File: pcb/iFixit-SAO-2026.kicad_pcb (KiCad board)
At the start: 2 copper layers, 82.6 x 83.8 mm, 29 parts, among them SW1 SW_Push, U1 ATtiny1604-SS

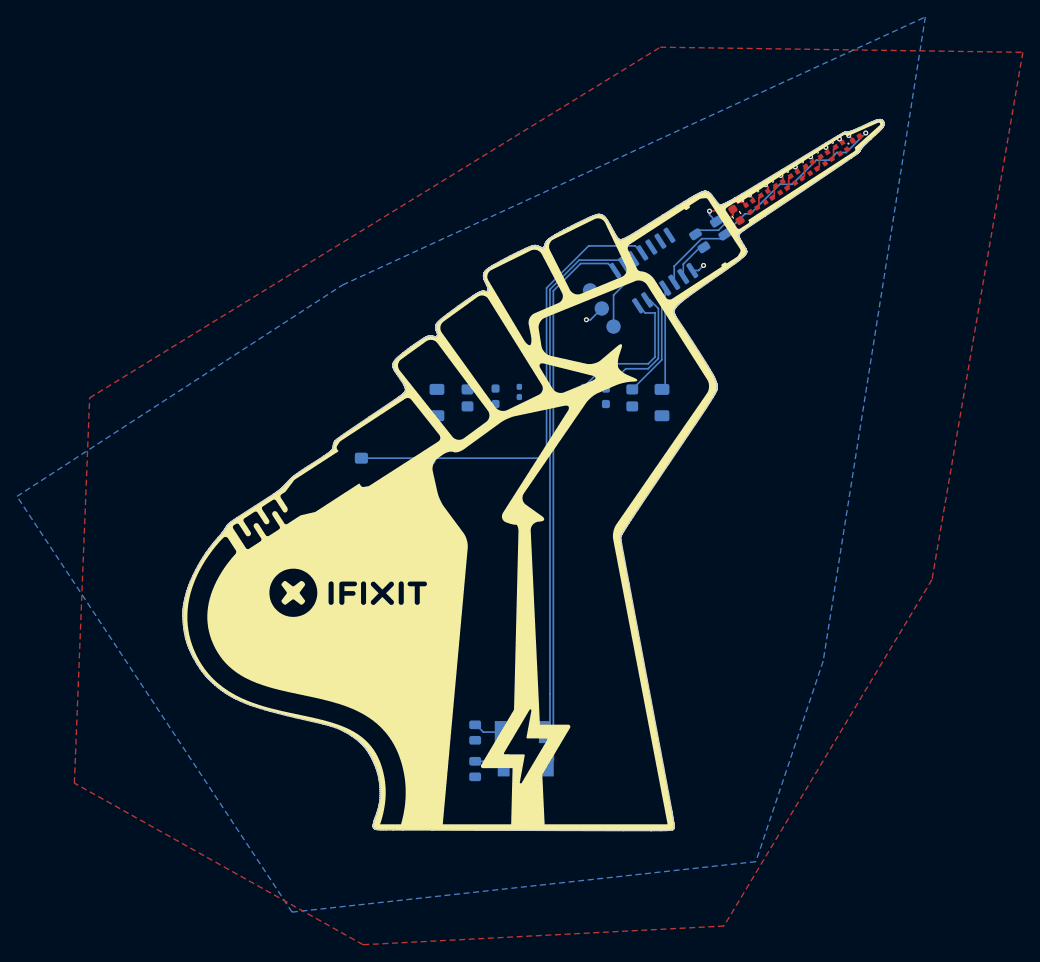
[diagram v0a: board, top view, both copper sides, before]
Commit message: Version 0.1 - FINAL: art, code, and PCB. 1000 made for DEFCON34
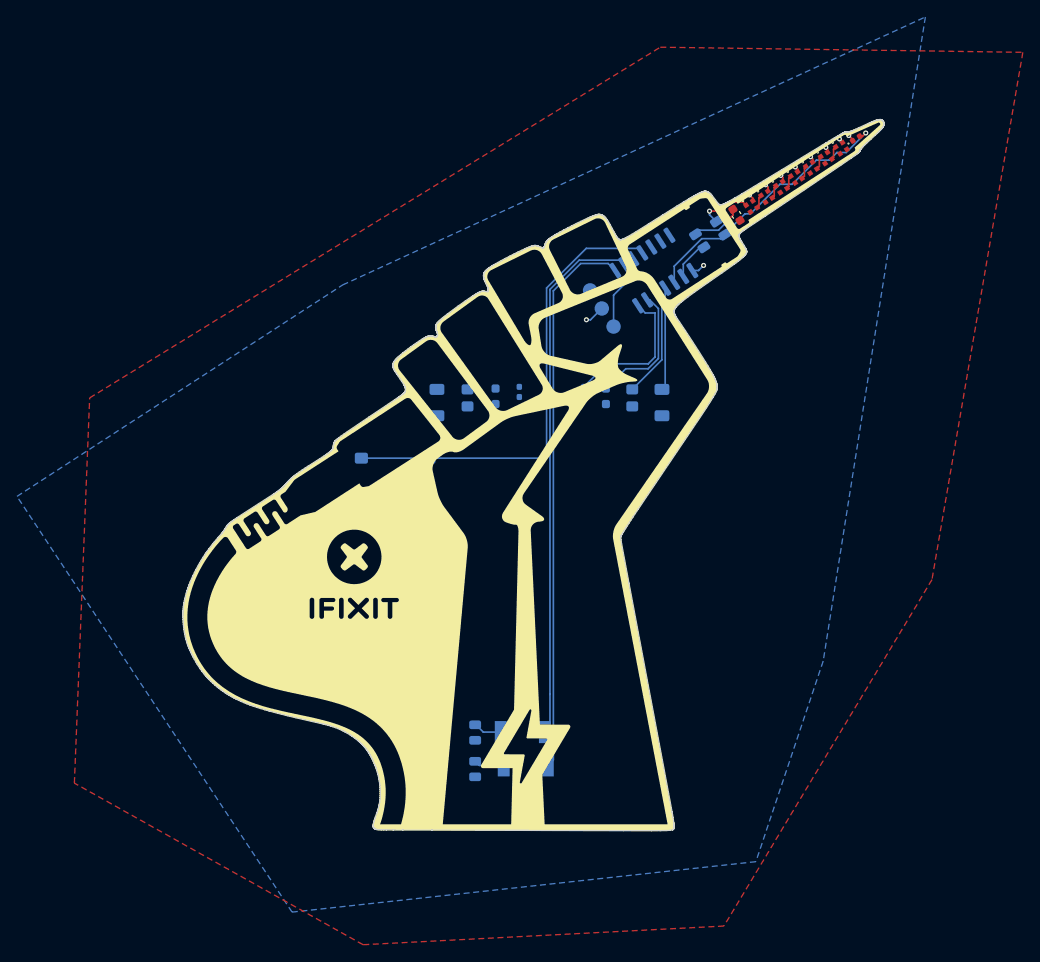
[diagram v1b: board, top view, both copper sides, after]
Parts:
- added G***: LOGO, LOGO, B.Cu at (148.3, 103.0)
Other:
- board text added: "v0.1"
- board text removed: "Move these..."
- board text removed: "Powering Your Right To Repair"
- board text removed: "for a treat."
- board text removed: "github.com/NerdFlare/iFixit-SAO-2026"
- board text removed: "ifixit.com/FixHub"
- board text removed: "over here..."
